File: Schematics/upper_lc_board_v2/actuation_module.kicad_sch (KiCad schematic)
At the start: 7 parts

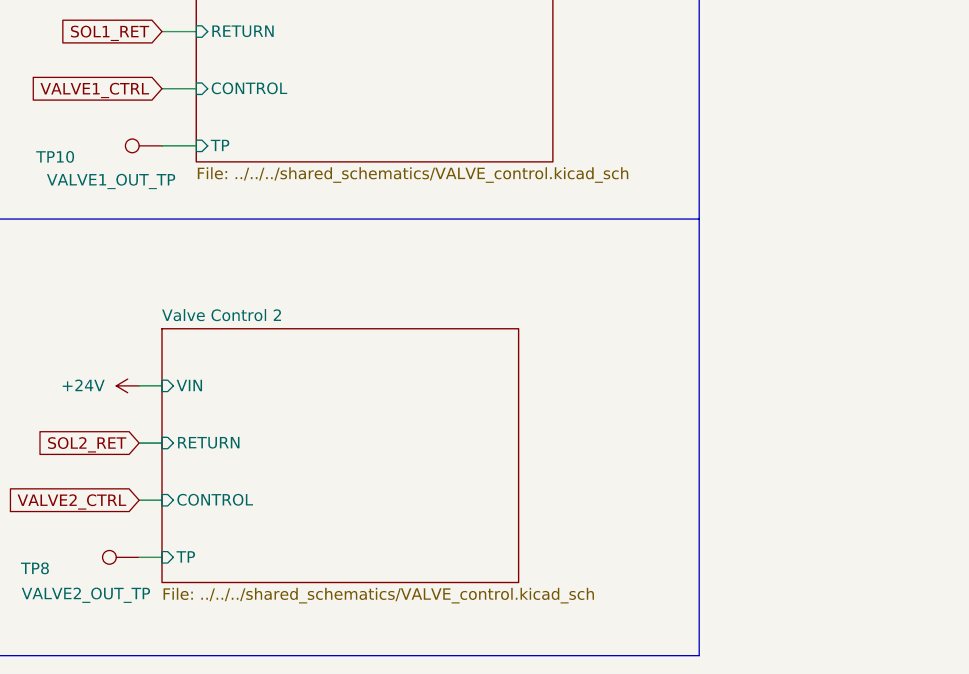
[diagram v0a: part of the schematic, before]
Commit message: layout updates after review, cleaned up schematic organization
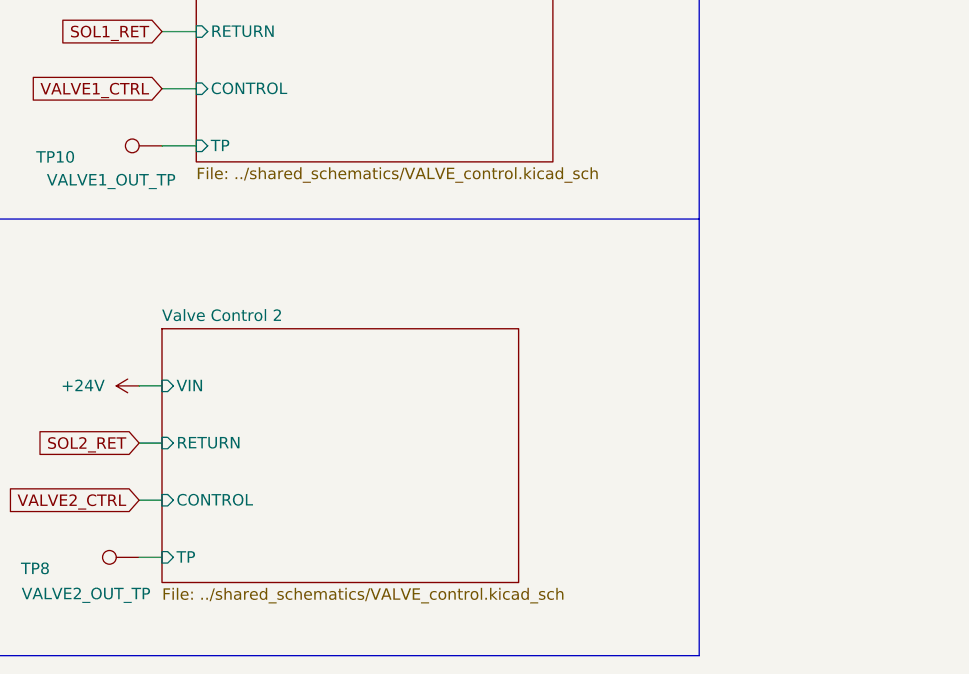
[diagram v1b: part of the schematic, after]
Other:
- sheet Valve Control 1: file ../../../shared_schematics/VALVE_control.kicad_sch -> ../shared_schematics/VALVE_control.kicad_sch
- sheet Valve Control 2: file ../../../shared_schematics/VALVE_control.kicad_sch -> ../shared_schematics/VALVE_control.kicad_sch
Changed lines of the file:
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@@
 			)
 		)
-		(property "Sheetfile" "../../../shared_schematics/VALVE_control.kicad_sch"
+		(property "Sheetfile" "../shared_schematics/VALVE_control.kicad_sch"
 			(at 168.91 86.1826 0)
 			(effects
@@
 			)
 		)
-		(property "Sheetfile" "../../../shared_schematics/VALVE_control.kicad_sch"
+		(property "Sheetfile" "../shared_schematics/VALVE_control.kicad_sch"
 			(at 165.1 132.9186 0)
 			(effects

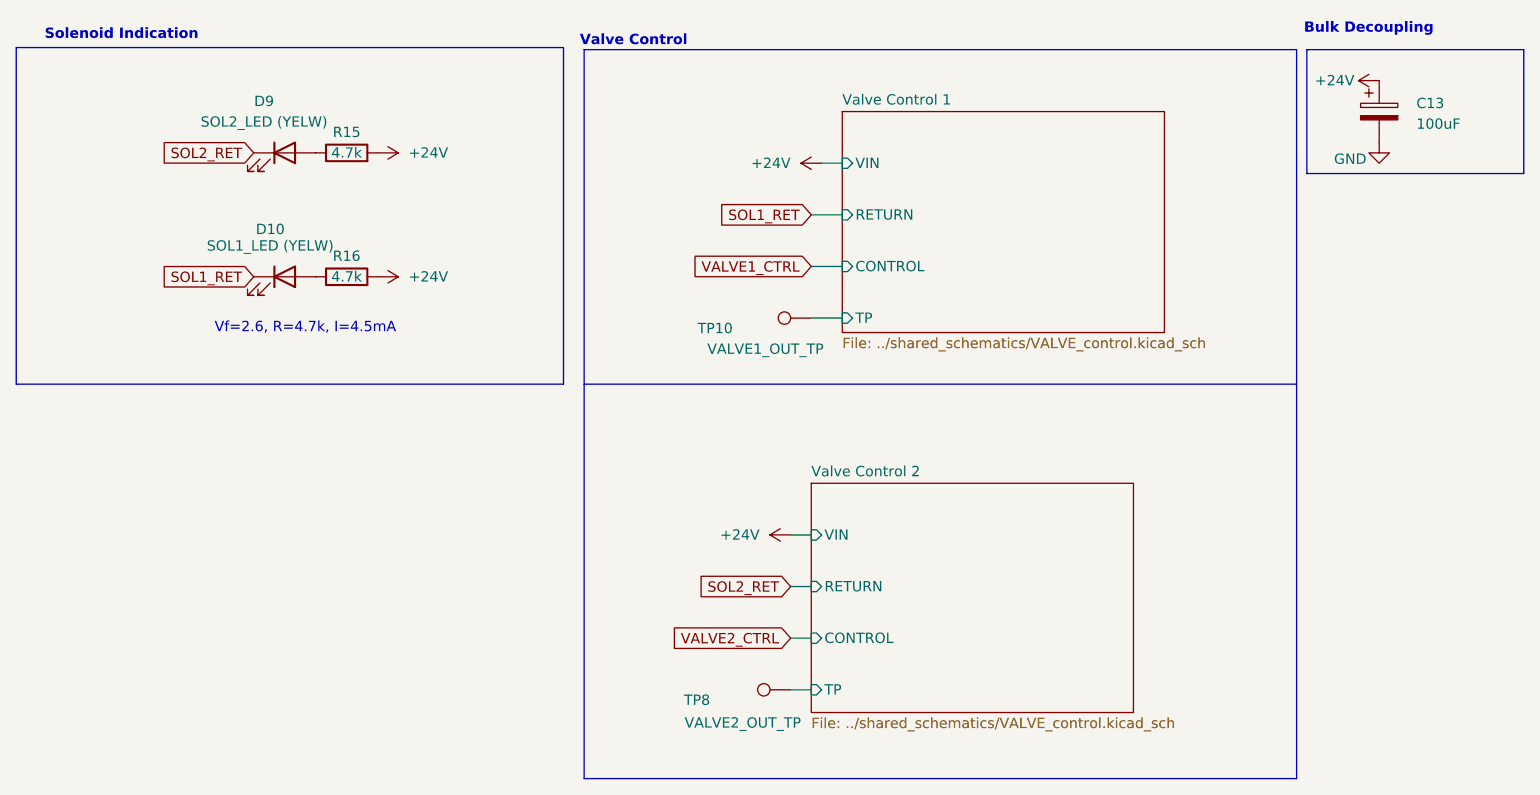
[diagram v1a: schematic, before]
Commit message: updated part numbers and fixed minor circuit issues
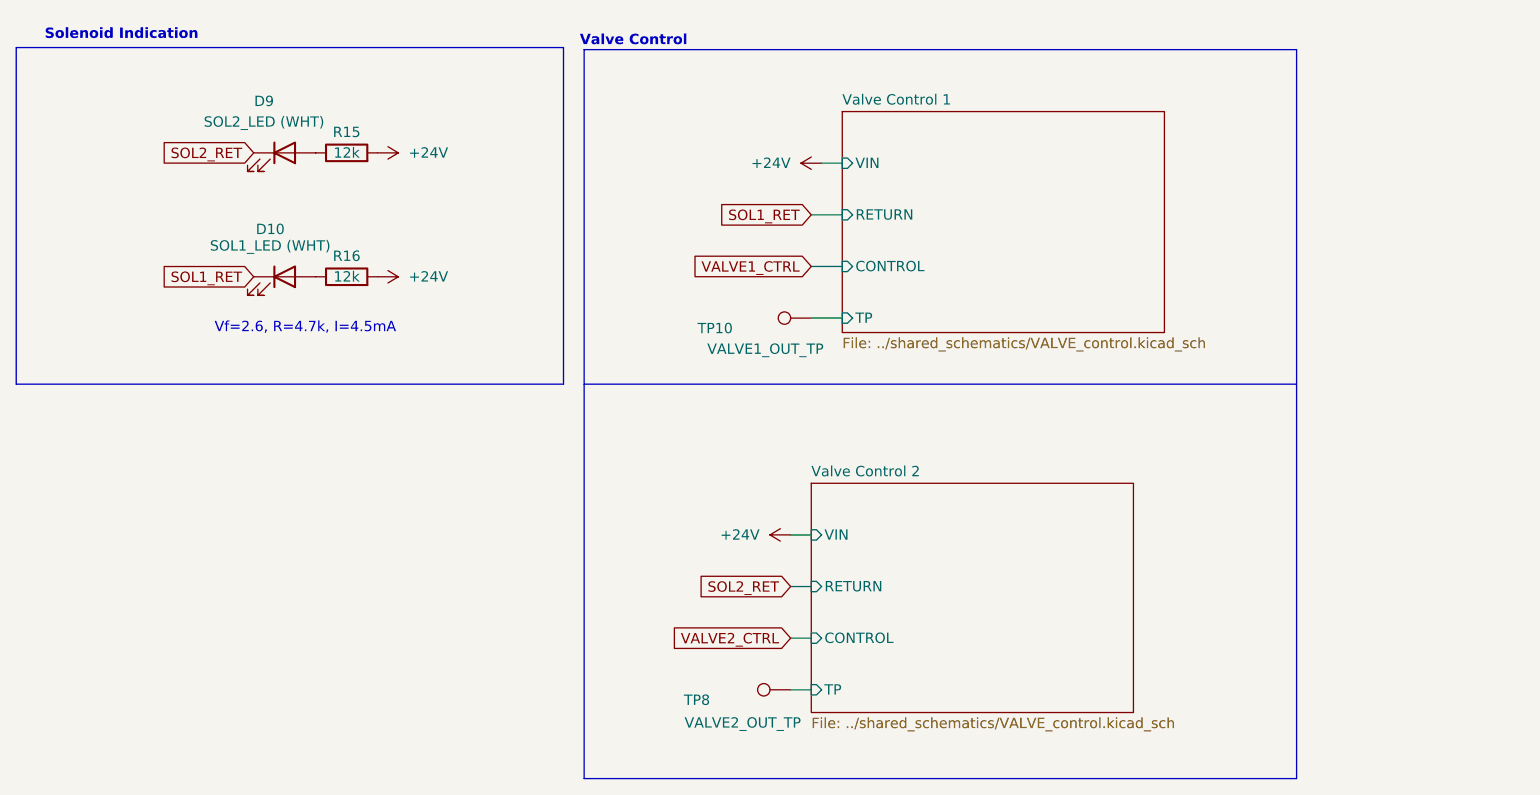
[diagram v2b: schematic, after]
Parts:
- removed C13: 100uF, Capacitor_SMD:CP_Elec_6.3x5.9, symbol Device:C_Polarized
- D10: value SOL1_LED (YELW) -> SOL1_LED (WHT)
- D9: value SOL2_LED (YELW) -> SOL2_LED (WHT)
- R15, R16: value 4.7k -> 12k; Digikey 311-4.70KFRCT-ND -> 311-12.1KFRCT-ND; JLCPCB C17936 -> (none); LCSC (none) -> C17912
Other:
- note removed: "Bulk Decoupling"
